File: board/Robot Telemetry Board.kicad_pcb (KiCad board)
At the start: 2 copper layers, 68 x 65 mm, 61 parts, among them J1 Conn_01x04, J2 Conn_01x04, J3 Conn_01x04, J4 Conn_01x04, J5 Conn_01x04, J6 Conn_01x02, J7 Conn_01x02, U1 Teensy4.1, U10 ADXL372, U2 TCMT1100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

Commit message: Completing the top half
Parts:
- U1: footprint teensy:Teensy41 -> teensy:Teensy41_DIP
- moved R17 4.11 mm to (161.8, 85.5)
- moved D2 4.10 mm to (165.0, 85.5)
- moved R19 3.91 mm to (161.8, 89.5)
- moved D4 3.90 mm to (165.0, 89.5)
- moved C1 0.77 mm to (111.0, 128.9)
- moved R18 0.25 mm to (161.8, 87.5)
- moved D3 0.13 mm to (165.0, 87.5)
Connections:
- R17 pad 1: unconnected-(R17-Pad1) -> /LED1
- R18 pad 1: unconnected-(R18-Pad1) -> /LED2
- R19 pad 1: unconnected-(R19-Pad1) -> /LED3
- U1 pad 1: GND -> unconnected-(U1-Pad1)
- U1 pad 29: unconnected-(U1-Pad29) -> /LED3
- U1 pad 30: unconnected-(U1-Pad30) -> /LED2
- U1 pad 31: unconnected-(U1-Pad31) -> /LED1
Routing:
- net /W_VESC2_UART3_RX: track 127.8 -> 42.6 mm, vias 1 -> 0
- net /D_VESC1_UART5_RX: track 0.00 -> 42.9 mm, vias 0 -> 1
- net /W_VESC2_UART3_TX: track 0.00 -> 42.3 mm
- net /SPI_MISO: track 0.82 -> 32.7 mm
- net /SPI_~{CS}: track 8.30 -> 38.5 mm, vias 0 -> 1
- net /LED1: track 0.00 -> 17.7 mm
- net /LED2: track 0.00 -> 14.4 mm
- net /SPI_SCK: track 4.58 -> 15.7 mm
- net /LED3: track 0.00 -> 11.1 mm
- net /SPI_MOSI: track 19.4 -> 30.4 mm, vias 1 -> 2
- net /ISO_UART1/VSS: track 28.1 -> 24.8 mm
- net +3V3: track 105.3 -> 102.0 mm
- net +5V: track 71.2 -> 68.1 mm
- net /ISO_UART1/VDD: track 5.98 -> 5.17 mm
- net GND: vias 1 -> 14

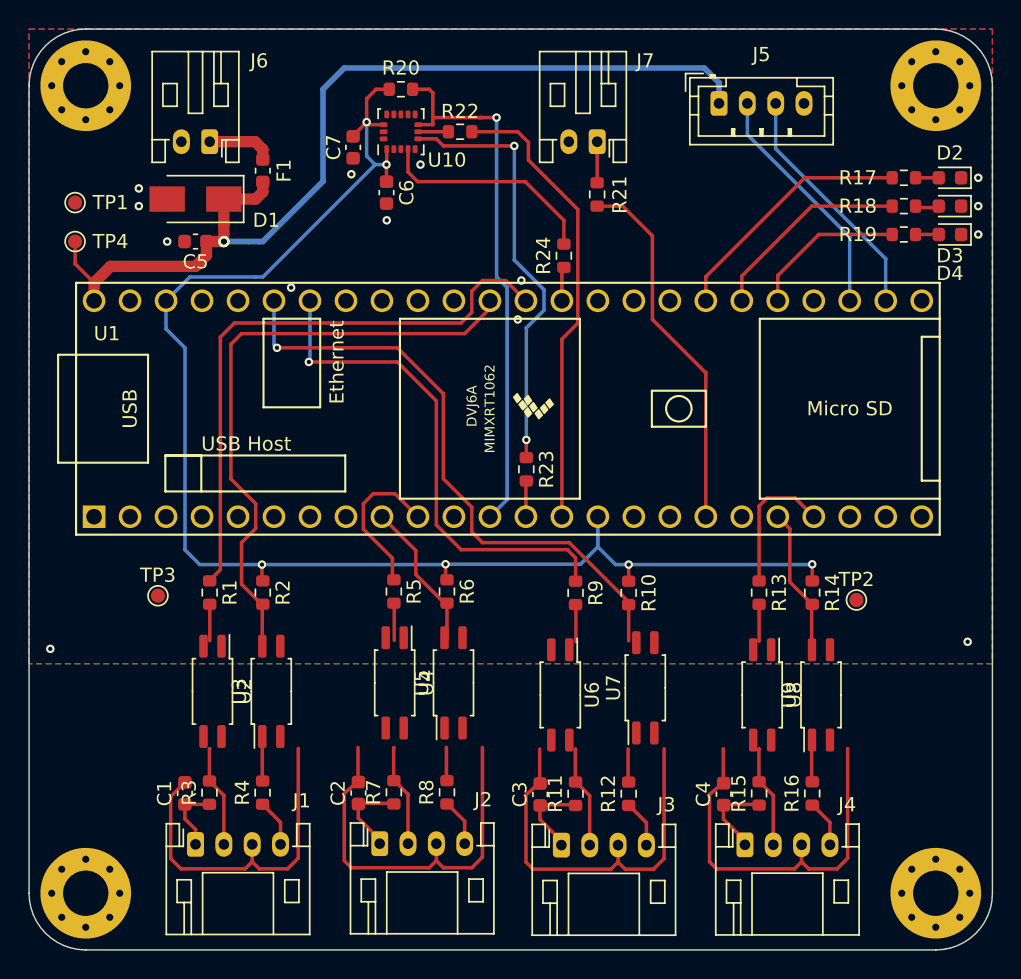
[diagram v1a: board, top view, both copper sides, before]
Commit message: updating optocouplers
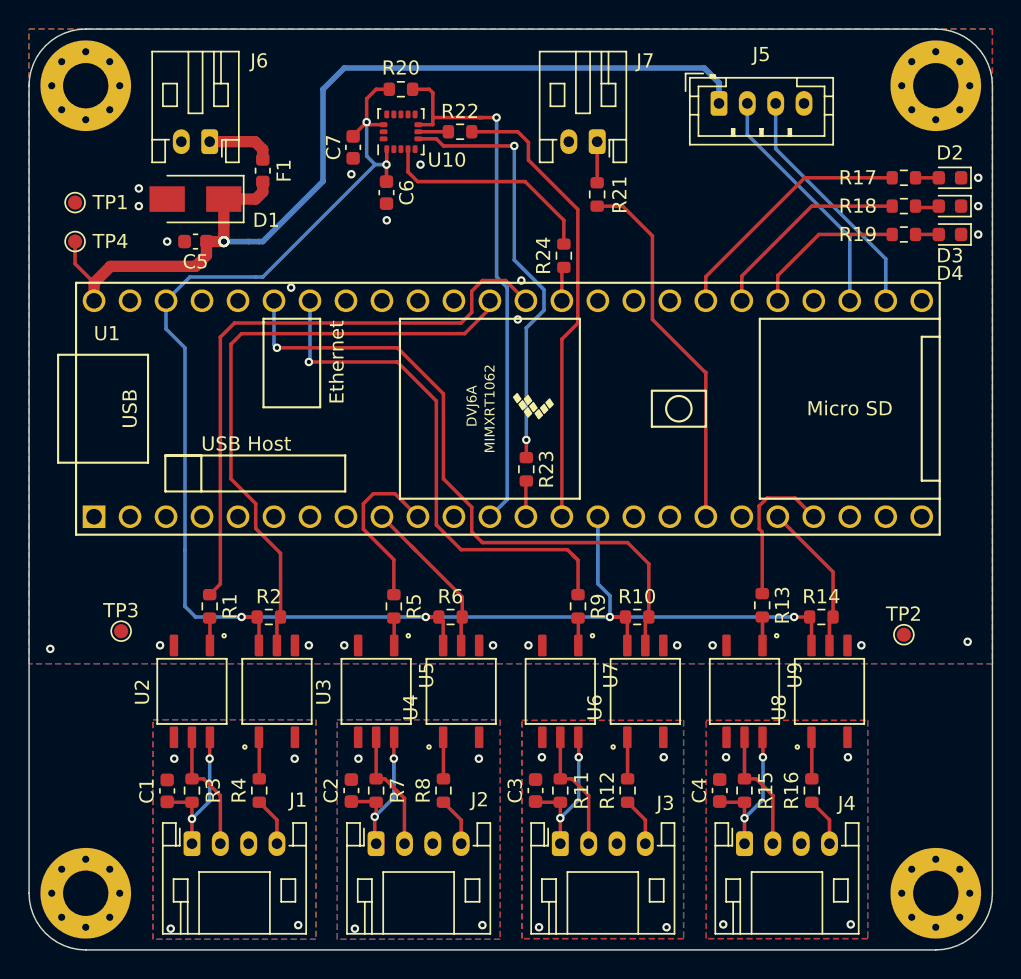
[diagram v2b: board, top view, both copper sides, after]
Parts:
- U2, U3, U4, U5, U6, U7, U8, U9: value TCMT1100 -> VOM452T; footprint Package_SO:SOP-4_4.4x2.6mm_P1.27mm -> VOM452T:SOIC127P700X230-5N
- moved U6 6.01 mm to (143.5, 121.8), turned to 90 degrees
- moved U7 6.01 mm to (137.5, 121.8), turned to -90 degrees
- moved U5 5.49 mm to (124.5, 121.8), turned to -90 degrees
- moved U9 5.41 mm to (150.5, 121.8), turned to -90 degrees
- moved U8 4.76 mm to (156.5, 121.8), turned to 90 degrees
- moved U4 4.73 mm to (130.5, 121.8), turned to 90 degrees
- moved TP2 4.15 mm to (161.8, 117.8)
- moved TP3 3.61 mm to (106.5, 117.5)
- moved R14 1.84 mm to (155.9, 116.5), turned to 0 degrees
- moved R6 1.82 mm to (129.8, 116.5), turned to 0 degrees
- moved R10 1.80 mm to (142.9, 116.5), turned to 0 degrees
- moved R2 1.78 mm to (116.9, 116.5), turned to 0 degrees
- moved U2 1.45 mm to (111.5, 121.8)
- moved C1 1.26 mm to (109.8, 128.8)
- moved R7 1.26 mm to (124.5, 128.8)
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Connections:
- U2 pad 3: /ISO_UART1/VSS -> GND
- U2 pad 4: /ISO_UART1/ISO_TX -> /ISO_UART1/VSS
- U3 pad 3: GND -> /ISO_UART1/VSS
- U3 pad 4: /W_VESC2_UART3_RX -> GND
- U4 pad 1: Net-(R5-Pad2) -> Net-(R8-Pad2)
- U4 pad 4: /ISO_UART2/ISO_TX -> GND
- U5 pad 1: Net-(R8-Pad2) -> Net-(R5-Pad2)
- U5 pad 4: /W_VESC1_UART2_RX -> /ISO_UART2/VSS
- U6 pad 1: Net-(R9-Pad2) -> Net-(R12-Pad2)
- U6 pad 4: /ISO_UART3/ISO_TX -> GND
- U7 pad 1: Net-(R12-Pad2) -> Net-(R9-Pad2)
- U7 pad 4: /D_VESC1_UART5_RX -> /ISO_UART3/VSS
- U8 pad 1: Net-(R13-Pad2) -> Net-(R16-Pad2)
- U8 pad 4: /ISO_UART4/ISO_TX -> GND
- U9 pad 1: Net-(R16-Pad2) -> Net-(R13-Pad2)
- U9 pad 4: /D_VESC2_UART7_RX -> /ISO_UART4/VSS
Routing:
- net /ISO_UART3/VSS: track 28.1 -> 0.00 mm, vias 0 -> 4
- net /ISO_UART2/VSS: track 28.1 -> 0.00 mm, vias 0 -> 4
- net /ISO_UART4/VSS: track 28.1 -> 0.00 mm, vias 0 -> 4
- net /ISO_UART1/VSS: track 24.8 -> 0.00 mm, vias 0 -> 4
- net +3V3: track 102.0 -> 116.7 mm
- net /ISO_UART1/VDD: track 5.17 -> 11.3 mm, vias 0 -> 2
- net /ISO_UART3/VDD: track 5.98 -> 11.3 mm, vias 0 -> 2
- net /ISO_UART4/VDD: track 5.98 -> 11.3 mm, vias 0 -> 2
- net /ISO_UART2/VDD: track 5.98 -> 10.9 mm, vias 0 -> 2
- net /D_VESC1_UART5_RX: track 42.9 -> 46.4 mm
- net /ISO_UART1/ISO_TX: track 7.21 -> 8.87 mm
- net /ISO_UART3/ISO_TX: track 7.21 -> 8.82 mm
- net /ISO_UART4/ISO_TX: track 7.21 -> 8.82 mm
- net /ISO_UART2/ISO_TX: track 7.21 -> 8.70 mm
- net /D_VESC1_UART5_TX: track 35.7 -> 37.0 mm
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- added copper zone on B.Cu, net /ISO_UART1/VSS
- added copper zone on F.Cu, net /ISO_UART1/VSS
- added copper zone on B.Cu, net /ISO_UART2/VSS
- added copper zone on F.Cu, net /ISO_UART2/VSS
- added copper zone on B.Cu, net /ISO_UART3/VSS
- added copper zone on F.Cu, net /ISO_UART3/VSS
- added copper zone on B.Cu, net /ISO_UART4/VSS
- added copper zone on F.Cu, net /ISO_UART4/VSS

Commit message: Adding LCSC part numbers
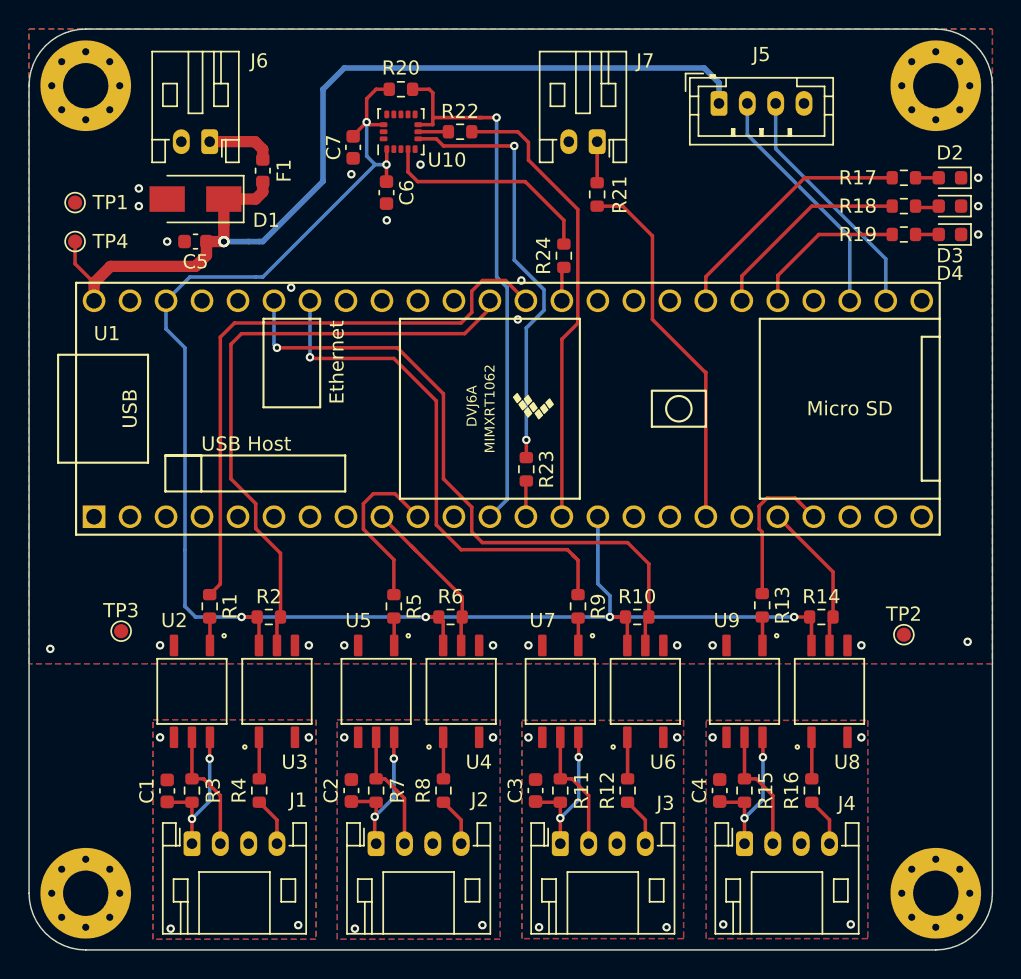
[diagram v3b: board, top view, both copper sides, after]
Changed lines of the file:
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@@
     (property "Sheetname" "ISO_UART2")
     (attr through_hole)
-    (fp_text reference "U5" (at -1.143255 -3.556805 -90) (layer "F.SilkS")
+    (fp_text reference "U5" (at -5 1.25) (layer "F.SilkS")
       (effects (font (size 1.000228 1.000228) (thickness 0.15)))
     )
@@
     (property "Sheetname" "ISO_UART4")
     (attr through_hole)
-    (fp_text reference "U9" (at -1.143255 -3.556805 -90) (layer "F.SilkS")
+    (fp_text reference "U9" (at -5 1.25) (layer "F.SilkS")
       (effects (font (size 1.000228 1.000228) (thickness 0.15)))
     )
@@
     (property "Sheetname" "ISO_UART2")
     (attr through_hole)
-    (fp_text reference "U4" (at -1.143255 -3.556805 90) (layer "F.SilkS")
+    (fp_text reference "U4" (at -5 1.25) (layer "F.SilkS")
       (effects (font (size 1.000228 1.000228) (thickness 0.15)))
     )
@@
     (property "Sheetname" "ISO_UART1")
     (attr through_hole)
-    (fp_text reference "U3" (at -0.05 3.3 90) (layer "F.SilkS")
+    (fp_text reference "U3" (at -5 1.25) (layer "F.SilkS")
       (effects (font (size 1.000228 1.000228) (thickness 0.15)))
     )
@@
     (property "Sheetname" "ISO_UART1")
     (attr through_hole)
-    (fp_text reference "U2" (at 0.05 3.5 -90) (layer "F.SilkS")
+    (fp_text reference "U2" (at -5 1.25 180) (layer "F.SilkS")
       (effects (font (size 1.000228 1.000228) (thickness 0.15)))
     )
@@
     (property "Sheetname" "ISO_UART4")
     (attr through_hole)
-    (fp_text reference "U8" (at -1.143255 -3.556805 90) (layer "F.SilkS")
+    (fp_text reference "U8" (at -5 1.25 180) (layer "F.SilkS")
       (effects (font (size 1.000228 1.000228) (thickness 0.15)))
     )
@@
     (property "Sheetname" "ISO_UART3")
     (attr through_hole)
-    (fp_text reference "U7" (at -1.143255 -3.556805 -90) (layer "F.SilkS")
+    (fp_text reference "U7" (at -5 1.25 180) (layer "F.SilkS")
       (effects (font (size 1.000228 1.000228) (thickness 0.15)))
     )
@@
     (property "Sheetname" "ISO_UART3")
     (attr through_hole)
-    (fp_text reference "U6" (at -1.143255 -3.556805 90) (layer "F.SilkS")
+    (fp_text reference "U6" (at -5 1.25 180) (layer "F.SilkS")
       (effects (font (size 1.000228 1.000228) (thickness 0.15)))
     )
@@
   (segment (start 112.75 126.5) (end 112.75 129.5) (width 0.25) (layer "B.Cu") (net 1))
   (segment (start 112.75 129.5) (end 111.5 130.75) (width 0.25) (layer "B.Cu") (net 1))
-  (via (at 118.75 126.5) (size 0.6) (drill 0.3) (layers "F.Cu" "B.Cu") (free) (net 2))
-  (via (at 110.25 126.5) (size 0.6) (drill 0.3) (layers "F.Cu" "B.Cu") (free) (net 2))
+  (via (at 119.75 125) (size 0.6) (drill 0.3) (layers "F.Cu" "B.Cu") (free) (net 2))
+  (via (at 109.25 125) (size 0.6) (drill 0.3) (layers "F.Cu" "B.Cu") (free) (net 2))
   (via (at 110 138.5) (size 0.6) (drill 0.3) (layers "F.Cu" "B.Cu") (free) (net 2))
   (via (at 119 138.25) (size 0.6) (drill 0.3) (layers "F.Cu" "B.Cu") (free) (net 2))
@@
   (via (at 132 138.25) (size 0.6) (drill 0.3) (layers "F.Cu" "B.Cu") (free) (net 4))
   (via (at 123 138.5) (size 0.6) (drill 0.3) (layers "F.Cu" "B.Cu") (free) (net 4))
-  (via (at 123.25 126.5) (size 0.6) (drill 0.3) (layers "F.Cu" "B.Cu") (free) (net 4))
-  (via (at 131.75 126.5) (size 0.6) (drill 0.3) (layers "F.Cu" "B.Cu") (free) (net 4))
+  (via (at 122.25 125) (size 0.6) (drill 0.3) (layers "F.Cu" "B.Cu") (free) (net 4))
+  (via (at 132.75 125) (size 0.6) (drill 0.3) (layers "F.Cu" "B.Cu") (free) (net 4))
   (segment (start 137.575 132.6) (end 137.575 132.3) (width 0.25) (layer "F.Cu") (net 5))
   (segment (start 138.8 126.4) (end 138.8 125.02) (width 0.25) (layer "F.Cu") (net 5))
@@
   (segment (start 137.5 130.7) (end 138.8 129.4) (width 0.25) (layer "B.Cu") (net 5))
   (segment (start 138.8 129.4) (end 138.8 126.4) (width 0.25) (layer "B.Cu") (net 5))
-  (via (at 136.2 126.4) (size 0.6) (drill 0.3) (layers "F.Cu" "B.Cu") (free) (net 6))
+  (via (at 135.25 125) (size 0.6) (drill 0.3) (layers "F.Cu" "B.Cu") (free) (net 6))
   (via (at 136 138.4) (size 0.6) (drill 0.3) (layers "F.Cu" "B.Cu") (free) (net 6))
-  (via (at 144.8 126.4) (size 0.6) (drill 0.3) (layers "F.Cu" "B.Cu") (free) (net 6))
+  (via (at 145.75 125) (size 0.6) (drill 0.3) (layers "F.Cu" "B.Cu") (free) (net 6))
   (via (at 145 138.4) (size 0.6) (drill 0.3) (layers "F.Cu" "B.Cu") (free) (net 6))
   (segment (start 112.77 116.595) (end 112.75 116.575) (width 0.25) (layer "F.Cu") (net 7))
@@
   (segment (start 150.5 130.7) (end 151.8 129.4) (width 0.25) (layer "B.Cu") (net 47))
   (segment (start 151.8 129.4) (end 151.8 126.4) (width 0.25) (layer "B.Cu") (net 47))
-  (via (at 157.8 126.4) (size 0.6) (drill 0.3) (layers "F.Cu" "B.Cu") (free) (net 48))
+  (via (at 158.75 125) (size 0.6) (drill 0.3) (layers "F.Cu" "B.Cu") (free) (net 48))
   (via (at 149 138.2) (size 0.6) (drill 0.3) (layers "F.Cu" "B.Cu") (free) (net 48))
-  (via (at 149.2 126.4) (size 0.6) (drill 0.3) (layers "F.Cu" "B.Cu") (free) (net 48))
+  (via (at 148.25 125) (size 0.6) (drill 0.3) (layers "F.Cu" "B.Cu") (free) (net 48))
   (via (at 158 138.2) (size 0.6) (drill 0.3) (layers "F.Cu" "B.Cu") (free) (net 48))
   (segment (start 150.5 127.925) (end 151.325 127.925) (width 0.25) (layer "F.Cu") (net 49))
@@
   (segment (start 117.75 116.5) (end 117.75 112) (width 0.25) (layer "F.Cu") (net 60))
   (segment (start 115 96.5) (end 130.75 96.5) (width 0.25) (layer "F.Cu") (net 60))
-  (segment (start 130.5 111.75) (end 138 111.75) (width 0.25) (layer "F.Cu") (net 61))
-  (segment (start 138 111.75) (end 138.375 112.125) (width 0.25) (layer "F.Cu") (net 61))
-  (segment (start 128.75 110) (end 130.5 111.75) (width 0.25) (layer "F.Cu") (net 61))
-  (segment (start 119.75 98.5) (end 126 98.5) (width 0.25) (layer "F.Cu") (net 61))
+  (segment (start 128.75 110) (end 128.75 101.25) (width 0.25) (layer "F.Cu") (net 61))
+  (segment (start 138 111.75) (end 130.5 111.75) (width 0.25) (layer "F.Cu") (net 61))
+  (segment (start 138.375 112.125) (end 138 111.75) (width 0.25) (layer "F.Cu") (net 61))
   (segment (start 138.75 112.5) (end 138.375 112.125) (width 0.25) (layer "F.Cu") (net 61))
-  (segment (start 128.75 101.25) (end 128.75 110) (width 0.25) (layer "F.Cu") (net 61))
+  (segment (start 130.5 111.75) (end 128.75 110) (width 0.25) (layer "F.Cu") (net 61))
+  (segment (start 125.75 98.25) (end 119.91 98.25) (width 0.25) (layer "F.Cu") (net 61))
+  (segment (start 119.91 98.25) (end 119.83 98.17) (width 0.25) (layer "F.Cu") (net 61))
   (segment (start 138.375 112.125) (end 138.575 112.325) (width 0.25) (layer "F.Cu") (net 61))
-  (segment (start 126 98.5) (end 128.75 101.25) (width 0.25) (layer "F.Cu") (net 61))
+  (segment (start 128.75 101.25) (end 125.75 98.25) (width 0.25) (layer "F.Cu") (net 61))
   (segment (start 138.75 114.925) (end 138.75 112.5) (width 0.25) (layer "F.Cu") (net 61))
-  (via (at 119.75 98.5) (size 0.6) (drill 0.3) (layers "F.Cu" "B.Cu") (net 61))
-  (segment (start 119.83 98.42) (end 119.75 98.5) (width 0.25) (layer "B.Cu") (net 61))
-  (segment (start 119.83 94.18) (end 119.83 98.42) (width 0.25) (layer "B.Cu") (net 61))
+  (via (at 119.83 98.17) (size 0.6) (drill 0.3) (layers "F.Cu" "B.Cu") (net 61))
+  (segment (start 119.83 94.18) (end 119.83 98.17) (width 0.25) (layer "B.Cu") (net 61))
   (segment (start 131.25 110.5) (end 131.25 108.75) (width 0.25) (layer "F.Cu") (net 62))
   (segment (start 129.25 100.75) (end 126 97.5) (width 0.25) (layer "F.Cu") (net 62))

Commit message: Adding some labels
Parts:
- added kibuzzard-61D772F0: G***, kibuzzard-61D772F0, F.Cu at (150.7, 86.5)
- added kibuzzard-61D7731E: G***, kibuzzard-61D7731E, F.Cu at (152.7, 86.5)
- added kibuzzard-61D77360: G***, kibuzzard-61D77360, F.Cu at (148.7, 86.5)
- added kibuzzard-61D7737B: G***, kibuzzard-61D7737B, F.Cu at (154.7, 86.5)
- added kibuzzard-61D7737B: G***, kibuzzard-61D7737B, F.Cu at (138.2, 87.0)
- added kibuzzard-61D773E1: G***, kibuzzard-61D773E1, F.Cu at (143.8, 82.2)
- added kibuzzard-61D773F7: G***, kibuzzard-61D773F7, F.Cu at (116.2, 80.8)
- added kibuzzard-61D7742A: G***, kibuzzard-61D7742A, F.Cu at (166.0, 99.2)
- added kibuzzard-61D77558: G***, kibuzzard-61D77558, F.Cu at (114.5, 130.5)
- added kibuzzard-61D77572: G***, kibuzzard-61D77572, F.Cu at (127.5, 130.8)
- added kibuzzard-61D7757F: G***, kibuzzard-61D7757F, F.Cu at (140.5, 130.8)
- added kibuzzard-61D77595: G***, kibuzzard-61D77595, F.Cu at (153.5, 130.5)
